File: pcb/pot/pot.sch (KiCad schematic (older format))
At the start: 26 parts, among them CON1 Valve, J1 Bus, J2 Bus, P1 Sensor, Q1 IRLZ44N, Q2 N7000, Q3 BS170, U1 PCF8574

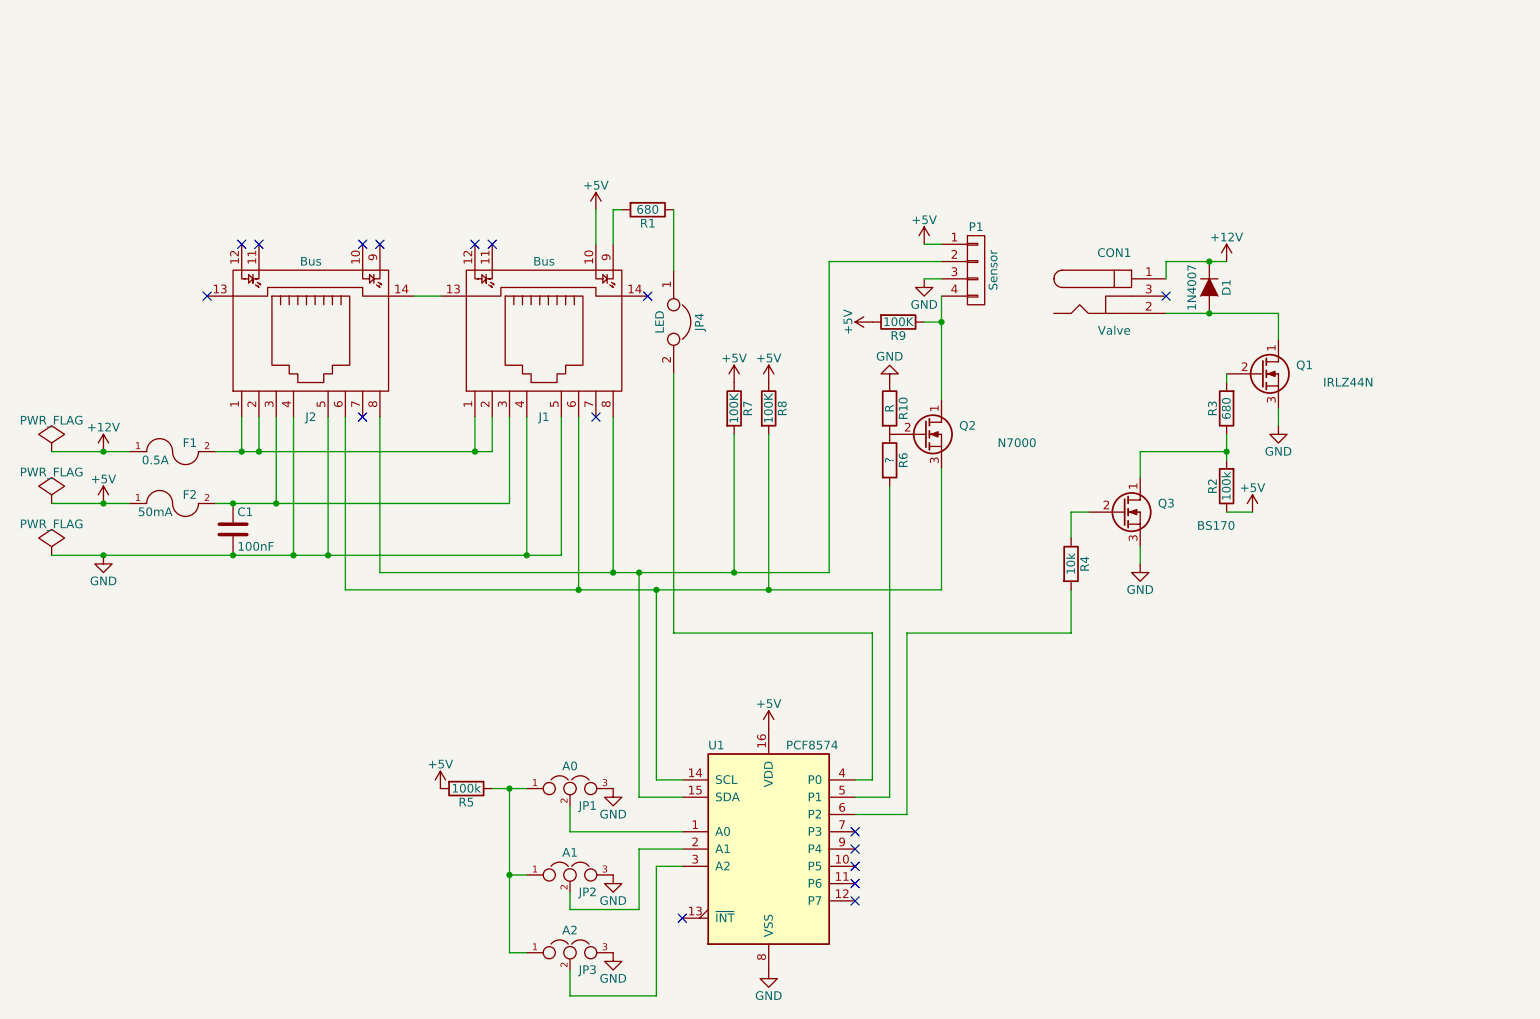
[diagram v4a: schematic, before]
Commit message: Use a MOSFET as bus switch
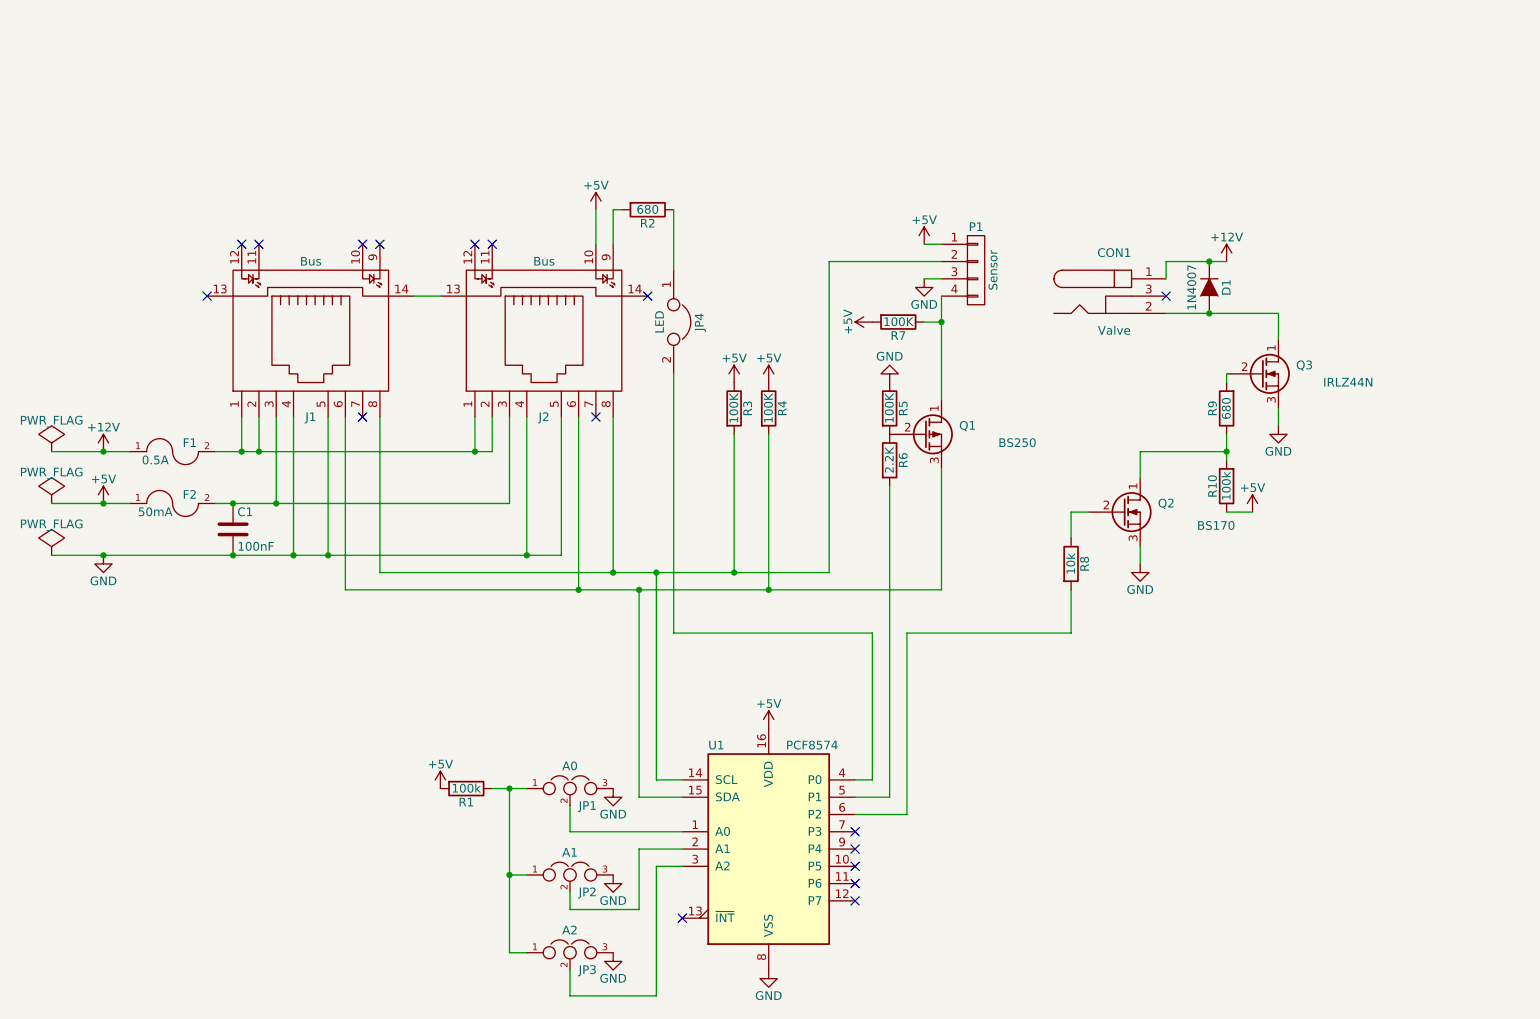
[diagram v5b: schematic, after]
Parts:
- removed Q2: N7000, symbol Q_NMOS_DGS
- added Q1: BS250, symbol Q_PMOS_DGS
- R5: renamed from R10; value R -> 100K
- R6: value ? -> 2.2K
- renumbered J2 to J1, J1 to J2, Q3 to Q2, Q1 to Q3, R5 to R1, R2 to R10, R1 to R2, R7 to R3, R8 to R4, R9 to R7, R4 to R8, R3 to R9
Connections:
- net at J1.6, J2.6, R4.2: now also U1.15 (SDA), Q1.3 (S); no longer U1.14 (SCL)
- net at J1.8, J2.8, P1.2 (P2)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: now also U1.14 (SCL); no longer U1.15 (SDA)
- net at P1.4 (P4), R7.1: now also Q1.1 (D)
- net at R5.2, R6.1: now also Q1.2 (G)
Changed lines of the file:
@@
 $EndDescr
 $Comp
-L RJ45_LEDS-RESCUE-pot-RESCUE-pot J1
+L RJ45_LEDS-RESCUE-pot-RESCUE-pot J2
 U 1 1 5951851F
 P 4250 2900
-F 0 "J1" H 4250 2400 50  0000 C CNN
+F 0 "J2" H 4250 2400 50  0000 C CNN
 F 1 "Bus" H 4250 3300 50  0000 C CNN
 F 2 "Connect:RJHSE538X" H 4250 2850 50  0001 C CNN
@@
 NoConn ~ 3950 2400
 $Comp
-L R R1
+L R R2
 U 1 1 595198B4
 P 4850 2200
-F 0 "R1" V 4930 2200 50  0000 C CNN
+F 0 "R2" V 4930 2200 50  0000 C CNN
 F 1 "680" V 4850 2200 50  0000 C CNN
 F 2 "Resistors_ThroughHole:R_Box_L13.0mm_W4.0mm_P9.00mm" V 4780 2200 50  0001 C CNN
@@
 $EndComp
 $Comp
-L R R4
+L R R8
 U 1 1 5951AE98
 P 7300 4250
-F 0 "R4" V 7380 4250 50  0000 C CNN
+F 0 "R8" V 7380 4250 50  0000 C CNN
 F 1 "10k" V 7300 4250 50  0000 C CNN
 F 2 "Resistors_ThroughHole:R_Box_L13.0mm_W4.0mm_P9.00mm" V 7230 4250 50  0001 C CNN
@@
 $EndComp
 $Comp
-L R R3
+L R R9
 U 1 1 5951B1C4
 P 8200 3350
-F 0 "R3" V 8280 3350 50  0000 C CNN
+F 0 "R9" V 8280 3350 50  0000 C CNN
 F 1 "680" V 8200 3350 50  0000 C CNN
 F 2 "Resistors_ThroughHole:R_Box_L13.0mm_W4.0mm_P9.00mm" V 8130 3350 50  0001 C CNN
@@
 $EndComp
 $Comp
-L R R2
+L R R10
 U 1 1 5951B3D8
 P 8200 3800
-F 0 "R2" V 8280 3800 50  0000 C CNN
+F 0 "R10" V 8280 3800 50  0000 C CNN
 F 1 "100k" V 8200 3800 50  0000 C CNN
 F 2 "Resistors_ThroughHole:R_Box_L13.0mm_W4.0mm_P9.00mm" V 8130 3800 50  0001 C CNN
@@
 $EndComp
 $Comp
-L Q_NMOS_DGS Q1
+L Q_NMOS_DGS Q3
 U 1 1 5951B683
 P 8400 3150
-F 0 "Q1" H 8700 3200 50  0000 R CNN
+F 0 "Q3" H 8700 3200 50  0000 R CNN
 F 1 "IRLZ44N" H 9050 3100 50  0000 R CNN
 F 2 "TO_SOT_Packages_THT:TO-220_Vertical" H 8600 3250 50  0001 C CNN
@@
 $EndComp
 $Comp
-L R R5
+L R R1
 U 1 1 59523656
 P 3800 5550
-F 0 "R5" V 3880 5550 50  0000 C CNN
+F 0 "R1" V 3880 5550 50  0000 C CNN
 F 1 "100k" V 3800 5550 50  0000 C CNN
 F 2 "Resistors_ThroughHole:R_Box_L13.0mm_W4.0mm_P9.00mm" V 3730 5550 50  0001 C CNN
@@
 P 6250 3650
 F 0 "R6" V 6330 3650 50  0000 C CNN
-F 1 "?" V 6250 3650 50  0000 C CNN
+F 1 "2.2K" V 6250 3650 50  0000 C CNN
 F 2 "Resistors_ThroughHole:R_Box_L13.0mm_W4.0mm_P9.00mm" V 6180 3650 50  0001 C CNN
 F 3 "" H 6250 3650 50  0000 C CNN
@@
 $EndComp
 $Comp
-L RJ45_LEDS-RESCUE-pot-RESCUE-pot J2
+L RJ45_LEDS-RESCUE-pot-RESCUE-pot J1
 U 1 1 59541C7B
 P 2900 2900
-F 0 "J2" H 2900 2400 50  0000 C CNN
+F 0 "J1" H 2900 2400 50  0000 C CNN
 F 1 "Bus" H 2900 3300 50  0000 C CNN
 F 2 "Connect:RJHSE538X" H 2900 2850 50  0001 C CNN
@@
 NoConn ~ 2300 2700
 $Comp
-L R R9
+L R R7
 U 1 1 595D0296
 P 6300 2850
-F 0 "R9" V 6380 2850 50  0000 C CNN
+F 0 "R7" V 6380 2850 50  0000 C CNN
 F 1 "100K" V 6300 2850 50  0000 C CNN
 F 2 "" V 6230 2850 50  0000 C CNN
@@
 $EndComp
 $Comp
-L R R7
+L R R3
 U 1 1 595D07D9
 P 5350 3350
-F 0 "R7" V 5430 3350 50  0000 C CNN
+F 0 "R3" V 5430 3350 50  0000 C CNN
 F 1 "100K" V 5350 3350 50  0000 C CNN
 F 2 "" V 5280 3350 50  0000 C CNN
@@
 $EndComp
 $Comp
-L R R8
+L R R4
 U 1 1 595D082E
 P 5550 3350
-F 0 "R8" V 5630 3350 50  0000 C CNN
+F 0 "R4" V 5630 3350 50  0000 C CNN
 F 1 "100K" V 5550 3350 50  0000 C CNN
 F 2 "" V 5480 3350 50  0000 C CNN
@@
 	6150 4650 5000 4650
 Wire Wire Line
-	4900 5500 5050 5500
-Wire Wire Line
-	4900 4400 4900 5500
-Connection ~ 4900 4400
-Wire Wire Line
-	5050 5600 4800 5600
-Wire Wire Line
-	4800 4300 4800 5600
-Connection ~ 4800 4300
-Wire Wire Line
 	4450 3400 4450 4400
 Connection ~ 4450 4400
@@
 $Comp
 L Q_NMOS_DGS Q2
-U 1 1 596E9EFF
-P 6450 3500
-F 0 "Q2" H 6750 3550 50  0000 R CNN
-F 1 "N7000" H 7100 3450 50  0000 R CNN
-F 2 "" H 6650 3600 50  0000 C CNN
-F 3 "" H 6450 3500 50  0000 C CNN
-	1    6450 3500
-	1    0    0    -1
-$EndComp
-$Comp
-L Q_NMOS_DGS Q3
 U 1 1 596EAFAD
 P 7600 3950
-F 0 "Q3" H 7900 4000 50  0000 R CNN
+F 0 "Q2" H 7900 4000 50  0000 R CNN
 F 1 "BS170" H 8250 3900 50  0000 R TNN
 F 2 "" H 7800 4050 50  0000 C CNN
@@
 $EndComp
 $Comp
-L R R10
+L R R5
 U 1 1 59706F50
 P 6250 3350
-F 0 "R10" V 6330 3350 50  0000 C CNN
-F 1 "R" V 6250 3350 50  0000 C CNN
+F 0 "R5" V 6330 3350 50  0000 C CNN
+F 1 "100K" V 6250 3350 50  0000 C CNN
 F 2 "" V 6180 3350 50  0000 C CNN
 F 3 "" H 6250 3350 50  0000 C CNN
@@
 Wire Wire Line
 	6350 5700 6050 5700
+$Comp
+L Q_PMOS_DGS Q1
+U 1 1 5B1B9224
+P 6450 3500
+F 0 "Q1" H 6750 3550 50  0000 R CNN
+F 1 "BS250" H 7100 3450 50  0000 R CNN
+F 2 "" H 6650 3600 50  0000 C CNN
+F 3 "" H 6450 3500 50  0000 C CNN
+	1    6450 3500
+	1    0    0    -1
+$EndComp
+Wire Wire Line
+	5050 5500 4900 5500
+Wire Wire Line
+	4900 5500 4900 4300
+Connection ~ 4900 4300
+Wire Wire Line
+	5050 5600 4800 5600
+Wire Wire Line
+	4800 5600 4800 4400
+Connection ~ 4800 4400
 $EndSCHEMATC
